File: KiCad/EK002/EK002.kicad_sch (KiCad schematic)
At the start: 80 parts, among them J1 BATT, J2 XKB_PJ-342B, SW1 D2FC, SW10 D2FC, SW11 D2FC, SW12 D2FC, SW13 D2FC, SW14 D2FC, SW15 D2FC, SW16 D2FC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

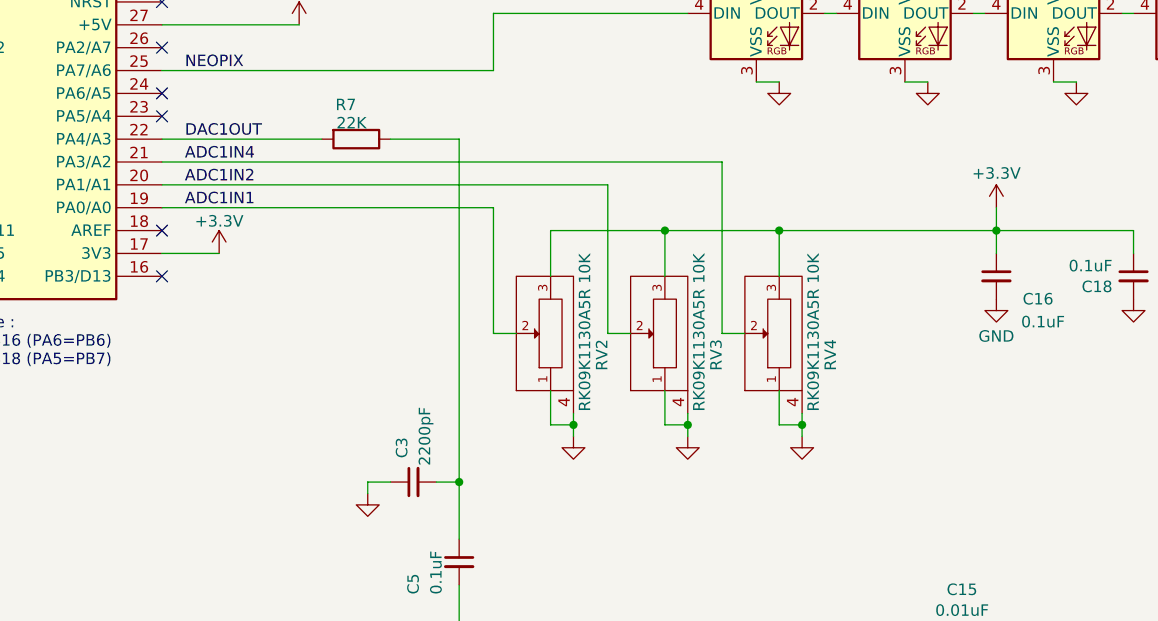
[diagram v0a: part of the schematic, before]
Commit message: update 3d model / software
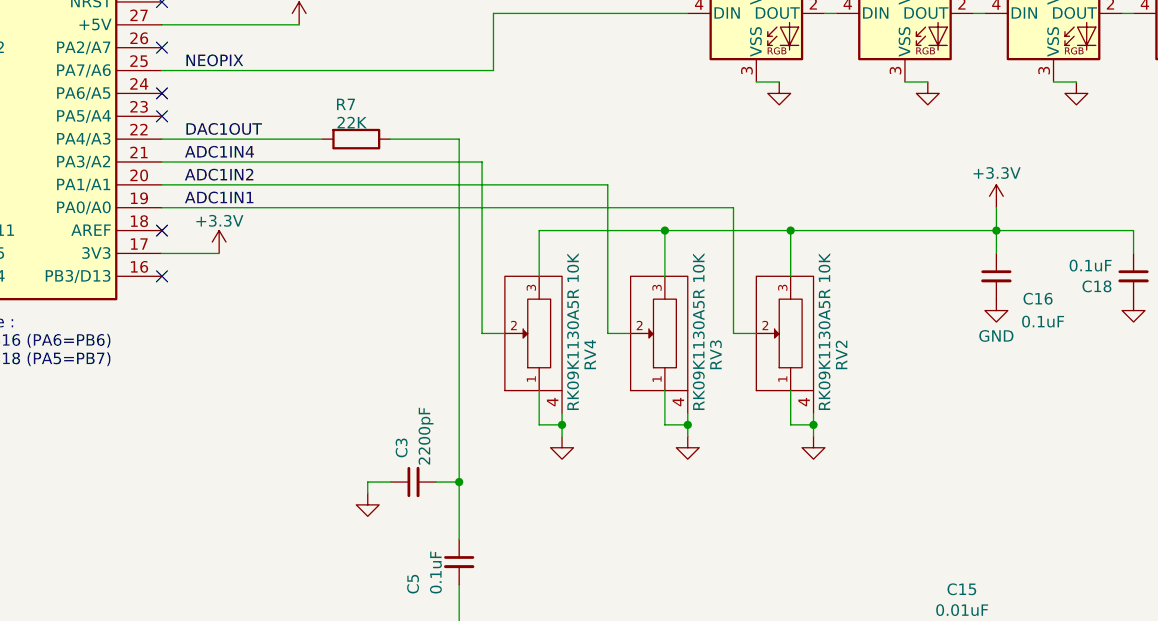
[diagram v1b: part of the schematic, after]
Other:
- moved on the sheet: RV2, RV4
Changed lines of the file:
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@@
   (title_block
     (title "ElectroKalimba EK-002")
-    (date "2023-12-03")
+    (date "2023-12-13")
     (rev "2.0.0")
     (company "g200kg")
   )
-  (junction (at 283.21 115.57) (diameter 0) (color 0 0 0 0)
+  (junction (at 309.88 115.57) (diameter 0) (color 0 0 0 0)
   )
   (junction (at 121.92 100.33) (diameter 0) (color 0 0 0 0)
@@
   (junction (at 137.16 185.42) (diameter 0) (color 0 0 0 0)
   )
+  (junction (at 293.37 93.98) (diameter 0) (color 0 0 0 0)
+  )
   (junction (at 303.53 60.96) (diameter 0) (color 0 0 0 0)
   )
   (junction (at 147.32 102.87) (diameter 0) (color 0 0 0 0)
   )
+  (junction (at 307.34 93.98) (diameter 0) (color 0 0 0 0)
+  )
   (junction (at 259.08 57.15) (diameter 0) (color 0 0 0 0)
   )
   (junction (at 246.38 57.15) (diameter 0) (color 0 0 0 0)
   )
-  (junction (at 293.37 93.98) (diameter 0) (color 0 0 0 0)
-  )
   (junction (at 292.1 212.09) (diameter 0) (color 0 0 0 0)
   )
@@
   (junction (at 132.08 110.49) (diameter 0) (color 0 0 0 0)
   )
-  (junction (at 306.07 93.98) (diameter 0) (color 0 0 0 0)
-  )
-  (junction (at 308.61 115.57) (diameter 0) (color 0 0 0 0)
+  (junction (at 281.94 115.57) (diameter 0) (color 0 0 0 0)
   )
   (junction (at 297.18 149.86) (diameter 0) (color 0 0 0 0)
@@
     (stroke (width 0) (type default))
   )
-  (wire (pts (xy 302.26 105.41) (xy 299.72 105.41))
+  (wire (pts (xy 275.59 105.41) (xy 273.05 105.41))
     (stroke (width 0) (type default))
   )
@@
     (stroke (width 0) (type default))
   )
-  (wire (pts (xy 280.67 115.57) (xy 280.67 111.76))
+  (wire (pts (xy 307.34 115.57) (xy 307.34 111.76))
     (stroke (width 0) (type default))
   )
@@
     (stroke (width 0) (type default))
   )
+  (wire (pts (xy 307.34 93.98) (xy 330.2 93.98))
+    (stroke (width 0) (type default))
+  )
   (wire (pts (xy 86.36 181.61) (xy 86.36 190.5))
     (stroke (width 0) (type default))
@@
     (stroke (width 0) (type default))
   )
-  (wire (pts (xy 299.72 105.41) (xy 299.72 86.36))
+  (wire (pts (xy 273.05 105.41) (xy 273.05 86.36))
     (stroke (width 0) (type default))
   )
@@
     (stroke (width 0) (type default))
   )
-  (wire (pts (xy 280.67 93.98) (xy 280.67 99.06))
+  (wire (pts (xy 307.34 93.98) (xy 307.34 99.06))
     (stroke (width 0) (type default))
   )
@@
     (stroke (width 0) (type default))
   )
-  (wire (pts (xy 237.49 91.44) (xy 274.32 91.44))
+  (wire (pts (xy 237.49 91.44) (xy 300.99 91.44))
     (stroke (width 0) (type default))
   )
@@
     (stroke (width 0) (type default))
   )
-  (wire (pts (xy 306.07 93.98) (xy 306.07 99.06))
+  (wire (pts (xy 279.4 93.98) (xy 279.4 99.06))
     (stroke (width 0) (type default))
   )
-  (wire (pts (xy 283.21 114.3) (xy 283.21 115.57))
+  (wire (pts (xy 309.88 114.3) (xy 309.88 115.57))
     (stroke (width 0) (type default))
   )
@@
     (stroke (width 0) (type default))
   )
-  (wire (pts (xy 308.61 115.57) (xy 308.61 116.84))
+  (wire (pts (xy 281.94 115.57) (xy 281.94 116.84))
     (stroke (width 0) (type default))
   )
@@
     (stroke (width 0) (type default))
   )
-  (wire (pts (xy 306.07 115.57) (xy 306.07 111.76))
+  (wire (pts (xy 279.4 115.57) (xy 279.4 111.76))
     (stroke (width 0) (type default))
   )
@@
     (stroke (width 0) (type default))
   )
-  (wire (pts (xy 308.61 115.57) (xy 306.07 115.57))
+  (wire (pts (xy 281.94 115.57) (xy 279.4 115.57))
     (stroke (width 0) (type default))
   )
@@
     (stroke (width 0) (type default))
   )
-  (wire (pts (xy 283.21 115.57) (xy 283.21 116.84))
+  (wire (pts (xy 309.88 115.57) (xy 309.88 116.84))
     (stroke (width 0) (type default))
   )
@@
     (stroke (width 0) (type default))
   )
-  (wire (pts (xy 308.61 114.3) (xy 308.61 115.57))
+  (wire (pts (xy 281.94 114.3) (xy 281.94 115.57))
     (stroke (width 0) (type default))
   )
@@
     (stroke (width 0) (type default))
   )
-  (wire (pts (xy 293.37 93.98) (xy 306.07 93.98))
-    (stroke (width 0) (type default))
-  )
   (wire (pts (xy 318.77 157.48) (xy 318.77 160.02))
     (stroke (width 0) (type default))
@@
     (stroke (width 0) (type default))
   )
-  (wire (pts (xy 274.32 105.41) (xy 276.86 105.41))
+  (wire (pts (xy 300.99 105.41) (xy 303.53 105.41))
     (stroke (width 0) (type default))
   )
@@
     (stroke (width 0) (type default))
   )
-  (wire (pts (xy 299.72 86.36) (xy 237.49 86.36))
+  (wire (pts (xy 273.05 86.36) (xy 237.49 86.36))
     (stroke (width 0) (type default))
   )
@@
     (stroke (width 0) (type default))
   )
-  (wire (pts (xy 280.67 93.98) (xy 293.37 93.98))
-    (stroke (width 0) (type default))
-  )
   (wire (pts (xy 314.96 186.69) (xy 314.96 189.23))
     (stroke (width 0) (type default))
@@
     (stroke (width 0) (type default))
   )
-  (wire (pts (xy 274.32 105.41) (xy 274.32 91.44))
+  (wire (pts (xy 300.99 105.41) (xy 300.99 91.44))
     (stroke (width 0) (type default))
   )
@@
     (stroke (width 0) (type default))
   )
+  (wire (pts (xy 293.37 93.98) (xy 307.34 93.98))
+    (stroke (width 0) (type default))
+  )
   (wire (pts (xy 259.08 66.04) (xy 259.08 57.15))
     (stroke (width 0) (type default))
@@
     (stroke (width 0) (type default))
   )
-  (wire (pts (xy 306.07 93.98) (xy 330.2 93.98))
-    (stroke (width 0) (type default))
-  )
   (wire (pts (xy 289.56 166.37) (xy 289.56 167.64))
     (stroke (width 0) (type default))
@@
     (stroke (width 0) (type default))
   )
-  (wire (pts (xy 283.21 115.57) (xy 280.67 115.57))
+  (wire (pts (xy 309.88 115.57) (xy 307.34 115.57))
     (stroke (width 0) (type default))
   )
@@
     (stroke (width 0) (type default))
   )
+  (wire (pts (xy 279.4 93.98) (xy 293.37 93.98))
+    (stroke (width 0) (type default))
+  )
   (wire (pts (xy 308.61 149.86) (xy 308.61 139.7))
     (stroke (width 0) (type default))
@@
     )
   )
-  (symbol (lib_id "power:GND") (at 308.61 116.84 0) (unit 1)
+  (symbol (lib_id "power:GND") (at 281.94 116.84 0) (unit 1)
     (in_bom yes) (on_board yes) (dnp no)
-    (property "Reference" "#PWR027" (at 308.61 123.19 0)
+    (property "Reference" "#PWR027" (at 281.94 123.19 0)
       (effects (font (size 1.27 1.27)) hide)
     )
-    (property "Value" "GND" (at 311.785 119.38 0)
+    (property "Value" "GND" (at 285.115 119.38 0)
       (effects (font (size 1.27 1.27)) hide)
     )
-    (property "Footprint" "" (at 308.61 116.84 0)
+    (property "Footprint" "" (at 281.94 116.84 0)
       (effects (font (size 1.27 1.27)) hide)
     )
-    (property "Datasheet" "" (at 308.61 116.84 0)
+    (property "Datasheet" "" (at 281.94 116.84 0)
       (effects (font (size 1.27 1.27)) hide)
     )
@@
     )
   )
-  (symbol (lib_id "power:GND") (at 283.21 116.84 0) (unit 1)
+  (symbol (lib_id "power:GND") (at 309.88 116.84 0) (unit 1)
     (in_bom yes) (on_board yes) (dnp no)
-    (property "Reference" "#PWR018" (at 283.21 123.19 0)
+    (property "Reference" "#PWR018" (at 309.88 123.19 0)
       (effects (font (size 1.27 1.27)) hide)
     )
-    (property "Value" "GND" (at 286.385 119.38 0)
+    (property "Value" "GND" (at 313.055 119.38 0)
       (effects (font (size 1.27 1.27)) hide)
     )
-    (property "Footprint" "" (at 283.21 116.84 0)
+    (property "Footprint" "" (at 309.88 116.84 0)
       (effects (font (size 1.27 1.27)) hide)
     )
-    (property "Datasheet" "" (at 283.21 116.84 0)
+    (property "Datasheet" "" (at 309.88 116.84 0)
       (effects (font (size 1.27 1.27)) hide)
     )
@@
     )
   )
-  (symbol (lib_id "MyLib:POT_G") (at 306.07 105.41 90) (unit 1)
+  (symbol (lib_id "MyLib:POT_G") (at 279.4 105.41 90) (unit 1)
     (in_bom yes) (on_board yes) (dnp no)
-    (property "Reference" "RV4" (at 311.785 106.045 0)
+    (property "Reference" "RV4" (at 285.115 106.045 0)
       (effects (font (size 1.27 1.27)) (justify right))
     )
-    (property "Value" "RK09K1130A5R 10K" (at 309.88 96.52 0)
+    (property "Value" "RK09K1130A5R 10K" (at 283.21 96.52 0)
       (effects (font (size 1.27 1.27)) (justify right))
     )
-    (property "Footprint" "MyLib:Potentiometer_Alps_RK09K_Single_Vertical" (at 306.07 105.41 0)
+    (property "Footprint" "MyLib:Potentiometer_Alps_RK09K_Single_Vertical" (at 279.4 105.41 0)
       (effects (font (size 1.27 1.27)) hide)
     )
-    (property "Datasheet" "" (at 306.07 105.41 0)
+    (property "Datasheet" "" (at 279.4 105.41 0)
       (effects (font (size 1.27 1.27)))
     )
@@
     )
   )
-  (symbol (lib_id "MyLib:POT_G") (at 280.67 105.41 90) (unit 1)
+  (symbol (lib_id "MyLib:POT_G") (at 307.34 105.41 90) (unit 1)
     (in_bom yes) (on_board yes) (dnp no)
-    (property "Reference" "RV2" (at 286.385 106.045 0)
+    (property "Reference" "RV2" (at 313.055 106.045 0)
       (effects (font (size 1.27 1.27)) (justify right))
     )
-    (property "Value" "RK09K1130A5R 10K" (at 284.48 96.52 0)
+    (property "Value" "RK09K1130A5R 10K" (at 311.15 96.52 0)
       (effects (font (size 1.27 1.27)) (justify right))
     )
-    (property "Footprint" "MyLib:Potentiometer_Alps_RK09K_Single_Vertical" (at 280.67 105.41 0)
+    (property "Footprint" "MyLib:Potentiometer_Alps_RK09K_Single_Vertical" (at 307.34 105.41 0)
       (effects (font (size 1.27 1.27)) hide)
     )
-    (property "Datasheet" "" (at 280.67 105.41 0)
+    (property "Datasheet" "" (at 307.34 105.41 0)
       (effects (font (size 1.27 1.27)))
     )
